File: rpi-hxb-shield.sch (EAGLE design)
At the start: 24 parts, among them Q1 CRYSTALX22, U2 24LC128-I/SN

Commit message: added comments to schematic
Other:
- note added: "I2C pull ups"
- note added: "Raspberry Pi connector"
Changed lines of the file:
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@@
 <text x="154.94" y="119.38" size="1.016" layer="97">wire antenna 85mm</text>
 <text x="119.38" y="43.18" size="1.016" layer="97">solder pads for antenna</text>
+<text x="152.4" y="48.26" size="1.016" layer="97">I2C pull ups</text>
+<text x="195.58" y="60.96" size="1.016" layer="97">Raspberry Pi connector</text>
 </plain>
 <instances>

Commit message: removed CLKM and according resistir
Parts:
- removed R1: 470R, rcl:R-EU_R0603
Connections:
- removed net CLKM: R1.1
- removed net N$5: R1.2, U1.CLKM
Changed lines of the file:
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@@
 <part name="C26" library="rcl" deviceset="C-EU" device="C0603" value="1uF"/>
 <part name="C27" library="rcl" deviceset="C-EU" device="C0603" value="1uF"/>
-<part name="R1" library="rcl" deviceset="R-EU_" device="R0603" value="470R"/>
 <part name="R3" library="rcl" deviceset="R-EU_" device="R0603" value="10k"/>
 <part name="U1" library="microbuilder" deviceset="AT86RF212" device=""/>
@@
 <instance part="C26" gate="G$1" x="149.86" y="160.02"/>
 <instance part="C27" gate="G$1" x="160.02" y="160.02"/>
-<instance part="R1" gate="G$1" x="43.18" y="91.44"/>
 <instance part="R3" gate="G$1" x="15.24" y="121.92" rot="R90"/>
 <instance part="U1" gate="G$1" x="83.82" y="109.22"/>
@@
 </segment>
 </net>
-<net name="N$5" class="0">
-<segment>
-<wire x1="53.34" y1="91.44" x2="48.26" y2="91.44" width="0.1524" layer="91"/>
-<pinref part="U1" gate="G$1" pin="CLKM"/>
-<pinref part="R1" gate="G$1" pin="2"/>
-</segment>
-</net>
-<net name="CLKM" class="0">
-<segment>
-<wire x1="38.1" y1="91.44" x2="33.02" y2="91.44" width="0.1524" layer="91"/>
-<label x="33.02" y="91.44" size="1.27" layer="95" rot="R180" xref="yes"/>
-<pinref part="R1" gate="G$1" pin="1"/>
-</segment>
-</net>

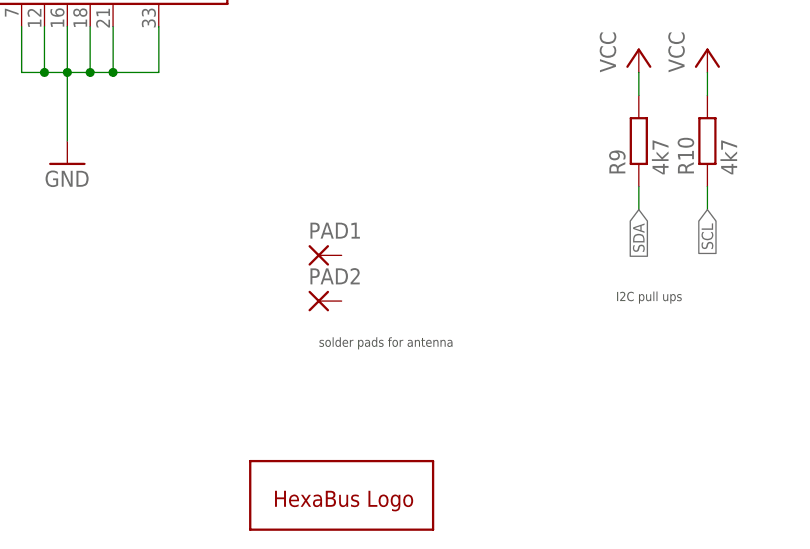
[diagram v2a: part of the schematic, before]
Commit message: maximum outline, removed wire antenna
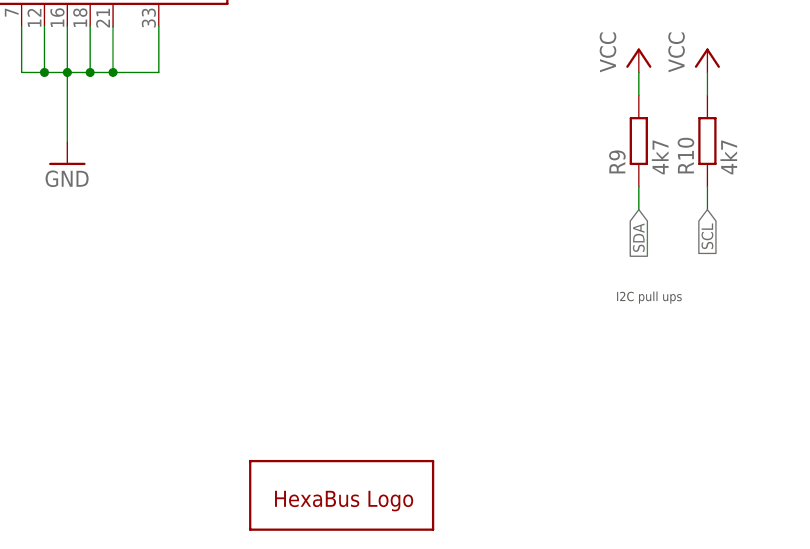
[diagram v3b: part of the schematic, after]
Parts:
- removed PAD1, PAD2: (no value), wirepad:SMD2
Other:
- note removed: "solder pads for antenna"
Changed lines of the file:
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@@
 <part name="P+8" library="supply1" deviceset="VCC" device=""/>
 <part name="P+9" library="supply1" deviceset="VCC" device=""/>
-<part name="PAD1" library="wirepad" deviceset="SMD2" device=""/>
-<part name="PAD2" library="wirepad" deviceset="SMD2" device=""/>
 <part name="U$1" library="artwork" deviceset="HEXAKRAKE" device=""/>
 <part name="U2" library="hexabus" deviceset="24LC128-I/SN" device=""/>
@@
 <text x="15.24" y="99.06" size="1.016" layer="91">GND for Q1</text>
 <text x="154.94" y="119.38" size="1.016" layer="97">wire antenna 85mm</text>
-<text x="119.38" y="43.18" size="1.016" layer="97">solder pads for antenna</text>
 <text x="152.4" y="48.26" size="1.016" layer="97">I2C pull ups</text>
 <text x="195.58" y="60.96" size="1.016" layer="97">Raspberry Pi connector</text>
@@
 <instance part="P+8" gate="VCC" x="15.24" y="144.78"/>
 <instance part="P+9" gate="VCC" x="88.9" y="172.72"/>
-<instance part="PAD1" gate="1" x="119.38" y="53.34"/>
-<instance part="PAD2" gate="1" x="119.38" y="48.26"/>
 <instance part="U$1" gate="G$1" x="111.76" y="22.86"/>
 <instance part="U2" gate="A" x="228.6" y="149.86"/>

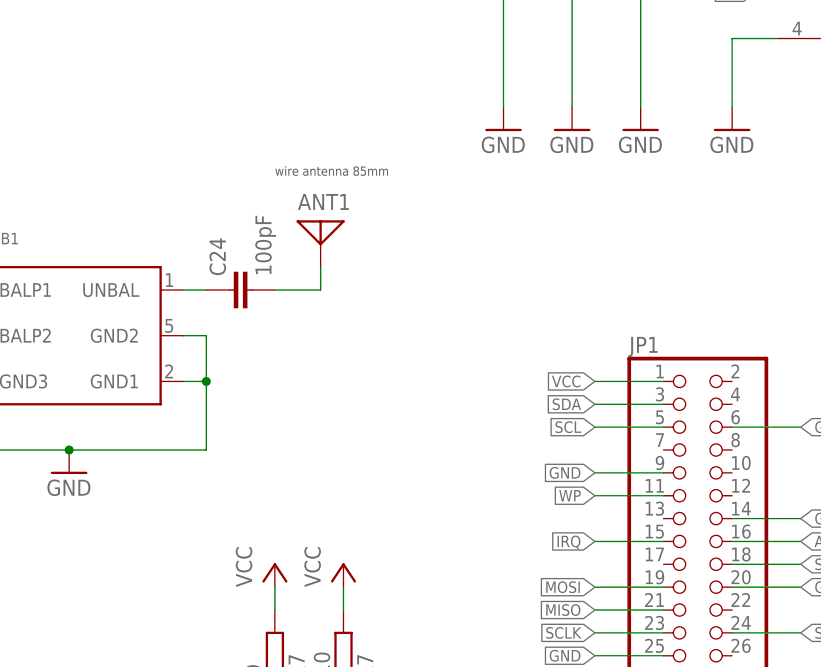
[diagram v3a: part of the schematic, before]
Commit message: changed resistors and capacitors to 0402, shuffled parts around
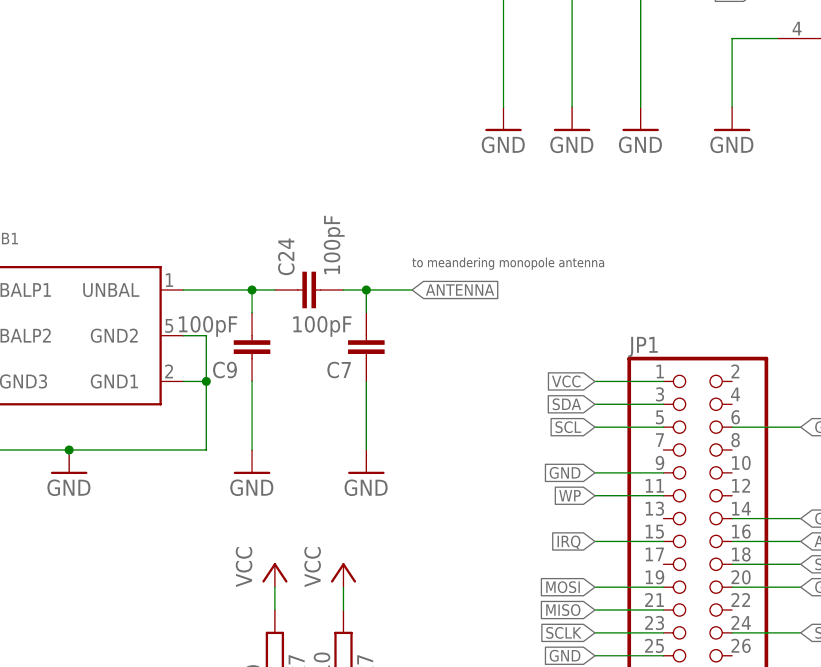
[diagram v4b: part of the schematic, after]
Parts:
- removed ANT1: (no value), discrete:ANTENNA
- added C7, C9: 100pF, rcl:C-EUC0402K
- C1, C13, C2, C24, C26, C27, C3, C4, C5, C6, C8: device rcl:C-EUC0603 -> rcl:C-EUC0402K
- R10, R3, R9: device rcl:R-EU_R0603 -> rcl:R-EU_R0402
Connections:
- removed net N$34: ANT1.1, C24.2
- new net ANTENNA: C24.2, C7.2
- net GND: now also C7.1, C9.1
- net N$33: now also C9.2
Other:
- note added: "to meandering monopole antenna"
- note removed: "wire antenna 85mm"
- moved on the sheet: C24
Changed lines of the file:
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@@
 <parts>
 <part name="FRAME1" library="frames" deviceset="A4L-LOC" device=""/>
-<part name="C13" library="rcl" deviceset="C-EU" device="C0603" value="220nF"/>
-<part name="C2" library="rcl" deviceset="C-EU" device="C0603" value="1uF"/>
-<part name="C3" library="rcl" deviceset="C-EU" device="C0603" value="1uF"/>
-<part name="C5" library="rcl" deviceset="C-EU" device="C0603" value="1uF"/>
-<part name="C6" library="rcl" deviceset="C-EU" device="C0603" value="1uF"/>
-<part name="C8" library="rcl" deviceset="C-EU" device="C0603" value="1uF"/>
-<part name="C24" library="rcl" deviceset="C-EU" device="C0603" value="100pF"/>
-<part name="C26" library="rcl" deviceset="C-EU" device="C0603" value="1uF"/>
-<part name="C27" library="rcl" deviceset="C-EU" device="C0603" value="1uF"/>
-<part name="R3" library="rcl" deviceset="R-EU_" device="R0603" value="10k"/>
+<part name="C13" library="rcl" deviceset="C-EU" device="C0402K" value="220nF"/>
+<part name="C2" library="rcl" deviceset="C-EU" device="C0402K" value="1uF"/>
+<part name="C3" library="rcl" deviceset="C-EU" device="C0402K" value="1uF"/>
+<part name="C5" library="rcl" deviceset="C-EU" device="C0402K" value="1uF"/>
+<part name="C6" library="rcl" deviceset="C-EU" device="C0402K" value="1uF"/>
+<part name="C8" library="rcl" deviceset="C-EU" device="C0402K" value="1uF"/>
+<part name="C24" library="rcl" deviceset="C-EU" device="C0402K" value="100pF"/>
+<part name="C26" library="rcl" deviceset="C-EU" device="C0402K" value="1uF"/>
+<part name="C27" library="rcl" deviceset="C-EU" device="C0402K" value="1uF"/>
+<part name="R3" library="rcl" deviceset="R-EU_" device="R0402" value="10k"/>
 <part name="U1" library="microbuilder" deviceset="AT86RF212" device=""/>
 <part name="GND1" library="supply1" deviceset="GND" device=""/>
@@
 <part name="GND7" library="supply1" deviceset="GND" device=""/>
 <part name="GND12" library="supply1" deviceset="GND" device=""/>
-<part name="ANT1" library="discrete" deviceset="ANTENNA" device=""/>
 <part name="B1" library="microbuilder" deviceset="BALUN+LP" device=""/>
 <part name="GND15" library="supply1" deviceset="GND" device=""/>
 <part name="GND16" library="supply1" deviceset="GND" device=""/>
 <part name="Q1" library="crystals-new" deviceset="CRYSTAL" device="X22"/>
-<part name="C1" library="rcl" deviceset="C-EU" device="C0603" value="18pF"/>
-<part name="C4" library="rcl" deviceset="C-EU" device="C0603" value="18pF"/>
+<part name="C1" library="rcl" deviceset="C-EU" device="C0402K" value="18pF"/>
+<part name="C4" library="rcl" deviceset="C-EU" device="C0402K" value="18pF"/>
 <part name="GND17" library="supply1" deviceset="GND" device=""/>
 <part name="P+5" library="supply1" deviceset="VCC" device=""/>
@@
 <part name="GND11" library="supply1" deviceset="GND" device=""/>
 <part name="JP1" library="pinhead" deviceset="PINHD-2X13" device=""/>
-<part name="R9" library="rcl" deviceset="R-EU_" device="R0603" value="4k7"/>
-<part name="R10" library="rcl" deviceset="R-EU_" device="R0603" value="4k7"/>
+<part name="R9" library="rcl" deviceset="R-EU_" device="R0402" value="4k7"/>
+<part name="R10" library="rcl" deviceset="R-EU_" device="R0402" value="4k7"/>
 <part name="P+7" library="supply1" deviceset="VCC" device=""/>
 <part name="P+10" library="supply1" deviceset="VCC" device=""/>
+<part name="C7" library="rcl" deviceset="C-EU" device="C0402K" value="100pF"/>
+<part name="C9" library="rcl" deviceset="C-EU" device="C0402K" value="100pF"/>
+<part name="GND13" library="supply1" deviceset="GND" device=""/>
+<part name="GND14" library="supply1" deviceset="GND" device=""/>
 </parts>
 <sheets>
@@
 <plain>
 <text x="15.24" y="99.06" size="1.016" layer="91">GND for Q1</text>
-<text x="154.94" y="119.38" size="1.016" layer="97">wire antenna 85mm</text>
+<text x="170.18" y="109.22" size="1.016" layer="97">to meandering monopole antenna</text>
 <text x="152.4" y="48.26" size="1.016" layer="97">I2C pull ups</text>
 <text x="195.58" y="60.96" size="1.016" layer="97">Raspberry Pi connector</text>
@@
 <instance part="C6" gate="G$1" x="66.04" y="144.78" rot="R270"/>
 <instance part="C8" gate="G$1" x="139.7" y="160.02"/>
-<instance part="C24" gate="G$1" x="149.86" y="106.68" rot="R90"/>
+<instance part="C24" gate="G$1" x="157.48" y="106.68" rot="R90"/>
 <instance part="C26" gate="G$1" x="149.86" y="160.02"/>
 <instance part="C27" gate="G$1" x="160.02" y="160.02"/>
@@
 <instance part="GND7" gate="1" x="15.24" y="111.76"/>
 <instance part="GND12" gate="1" x="149.86" y="147.32"/>
-<instance part="ANT1" gate="A" x="160.02" y="114.3"/>
 <instance part="B1" gate="G$1" x="132.08" y="101.6" rot="R270"/>
 <instance part="GND15" gate="1" x="132.08" y="86.36"/>
@@
 <instance part="P+7" gate="VCC" x="154.94" y="76.2"/>
 <instance part="P+10" gate="VCC" x="162.56" y="76.2"/>
+<instance part="C7" gate="G$1" x="165.1" y="99.06" rot="R180"/>
+<instance part="C9" gate="G$1" x="152.4" y="99.06" rot="R180"/>
+<instance part="GND13" gate="1" x="152.4" y="86.36"/>
+<instance part="GND14" gate="1" x="165.1" y="86.36"/>
 </instances>
 <busses>
@@
 <wire x1="180.34" y1="152.4" x2="210.82" y2="152.4" width="0.1524" layer="91"/>
 </segment>
+<segment>
+<pinref part="GND14" gate="1" pin="GND"/>
+<pinref part="C7" gate="G$1" pin="1"/>
+<wire x1="165.1" y1="88.9" x2="165.1" y2="96.52" width="0.1524" layer="91"/>
+</segment>
+<segment>
+<pinref part="GND13" gate="1" pin="GND"/>
+<pinref part="C9" gate="G$1" pin="1"/>
+<wire x1="152.4" y1="88.9" x2="152.4" y2="96.52" width="0.1524" layer="91"/>
+</segment>
 </net>
 <net name="IRQ" class="0">
@@
 <net name="N$33" class="0">
 <segment>
-<wire x1="144.78" y1="106.68" x2="147.32" y2="106.68" width="0.1524" layer="91"/>
+<wire x1="144.78" y1="106.68" x2="152.4" y2="106.68" width="0.1524" layer="91"/>
 <pinref part="B1" gate="G$1" pin="UNBAL"/>
 <pinref part="C24" gate="G$1" pin="1"/>
-</segment>
-</net>
-<net name="N$34" class="0">
-<segment>
-<wire x1="154.94" y1="106.68" x2="160.02" y2="106.68" width="0.1524" layer="91"/>
-<wire x1="160.02" y1="106.68" x2="160.02" y2="109.22" width="0.1524" layer="91"/>
+<pinref part="C9" gate="G$1" pin="2"/>
+<wire x1="152.4" y1="106.68" x2="154.94" y2="106.68" width="0.1524" layer="91"/>
+<wire x1="152.4" y1="104.14" x2="152.4" y2="106.68" width="0.1524" layer="91"/>
+<junction x="152.4" y="106.68"/>
+</segment>
+</net>
+<net name="ANTENNA" class="0">
+<segment>
+<wire x1="162.56" y1="106.68" x2="165.1" y2="106.68" width="0.1524" layer="91"/>
 <pinref part="C24" gate="G$1" pin="2"/>
-<pinref part="ANT1" gate="A" pin="1"/>
-</segment>
-</net>
+<label x="170.18" y="106.68" size="1.27" layer="95" xref="yes"/>
+<pinref part="C7" gate="G$1" pin="2"/>
+<wire x1="165.1" y1="106.68" x2="170.18" y2="106.68" width="0.1524" layer="91"/>
+<wire x1="165.1" y1="104.14" x2="165.1" y2="106.68" width="0.1524" layer="91"/>
+<junction x="165.1" y="106.68"/>
+</segment>
+</net>

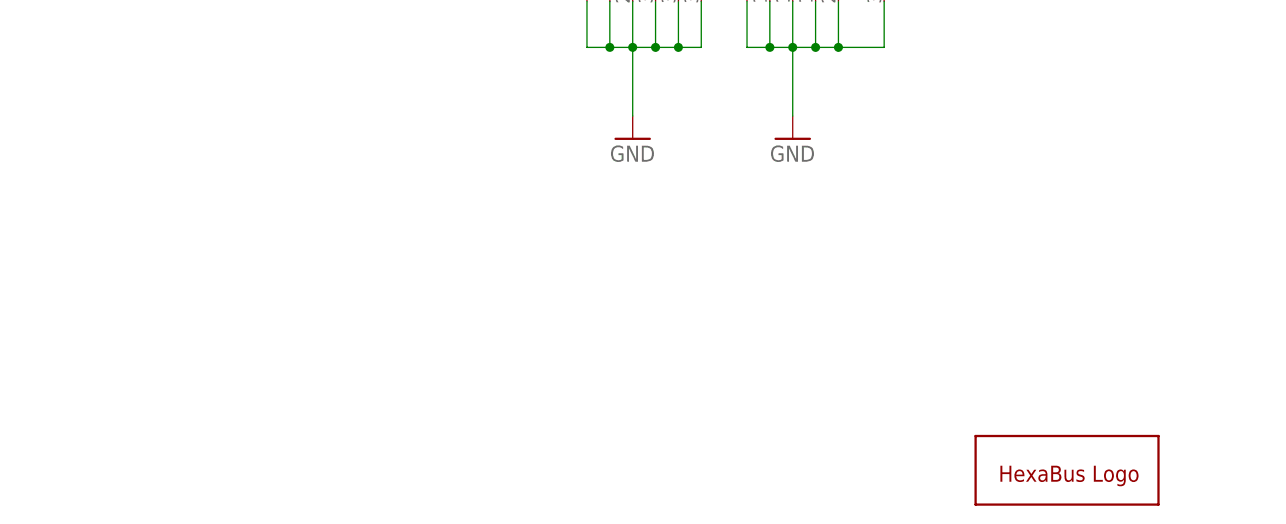
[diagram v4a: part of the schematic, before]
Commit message: added note for excluded parts
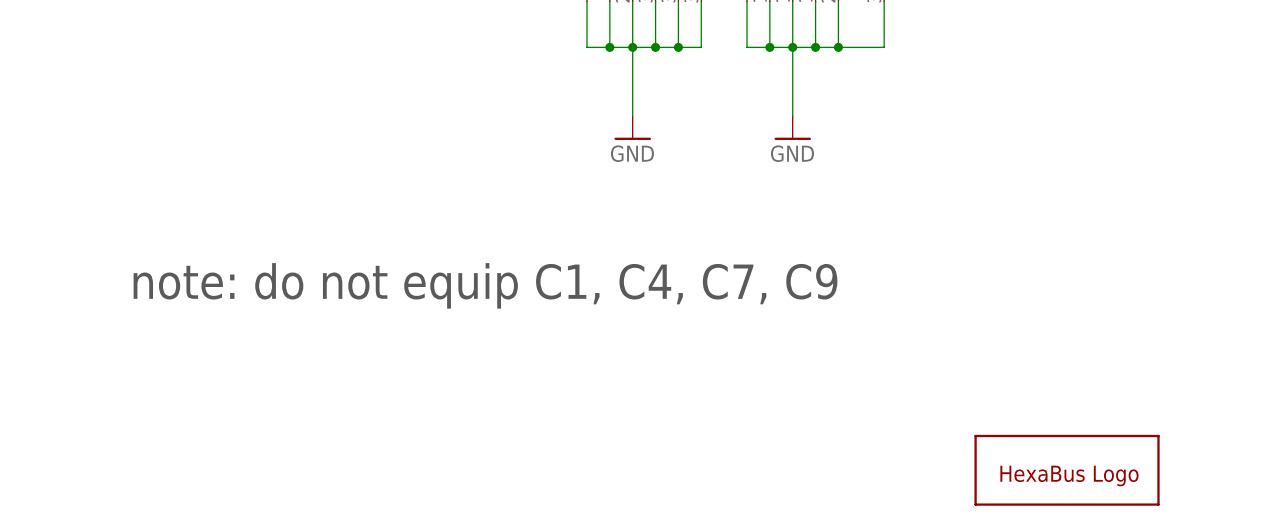
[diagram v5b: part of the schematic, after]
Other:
- note added: "note: do not equip C1, C4, C7, C9"
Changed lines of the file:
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@@
 <text x="152.4" y="48.26" size="1.016" layer="97">I2C pull ups</text>
 <text x="195.58" y="60.96" size="1.016" layer="97">Raspberry Pi connector</text>
+<text x="17.78" y="45.72" size="3.81" layer="97">note: do not equip C1, C4, C7, C9</text>
 </plain>
 <instances>
